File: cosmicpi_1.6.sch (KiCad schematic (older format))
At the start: 95 parts, among them J1 Barrel_Jack_Switch, J2 SMA, J3 USB_B_Micro, J6 SWD, J7 Raspberry_Pi_2_3, U1 MCP47CMB22, U10 TPS62163DSG, U11 LM555, U12 LM555, U16 LP2985-3.3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

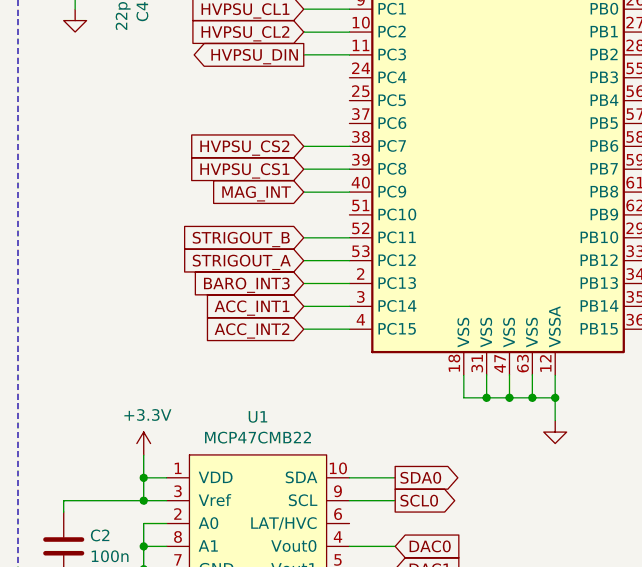
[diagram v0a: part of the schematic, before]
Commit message: Incorporated comments from TE-MPE
They kindly checked the layout and schematic over for us! Can't be sure we got all the bugs until we build it though. Reversed raspberry pi header so that the connection will be inside the enclosure.
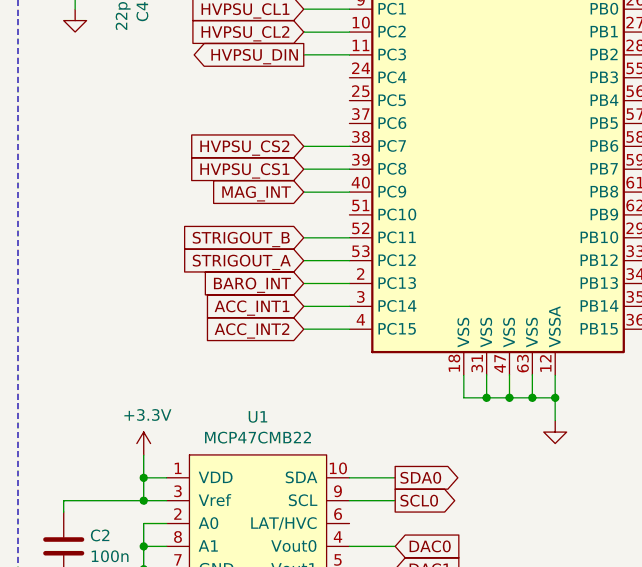
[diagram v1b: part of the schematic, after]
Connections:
- net BARO_INT3 is gone; now on net BARO_INT: U2.2 (PC13)
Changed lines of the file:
@@
 STRIGOUT_B
 Text GLabel 1900 4900 0    50   Input ~ 0
-BARO_INT3
+BARO_INT
 Text GLabel 3700 2400 2    50   Output ~ 0
 LED1
